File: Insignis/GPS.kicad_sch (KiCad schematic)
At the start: 4 parts, among them IC6 MAX-M10S-00B

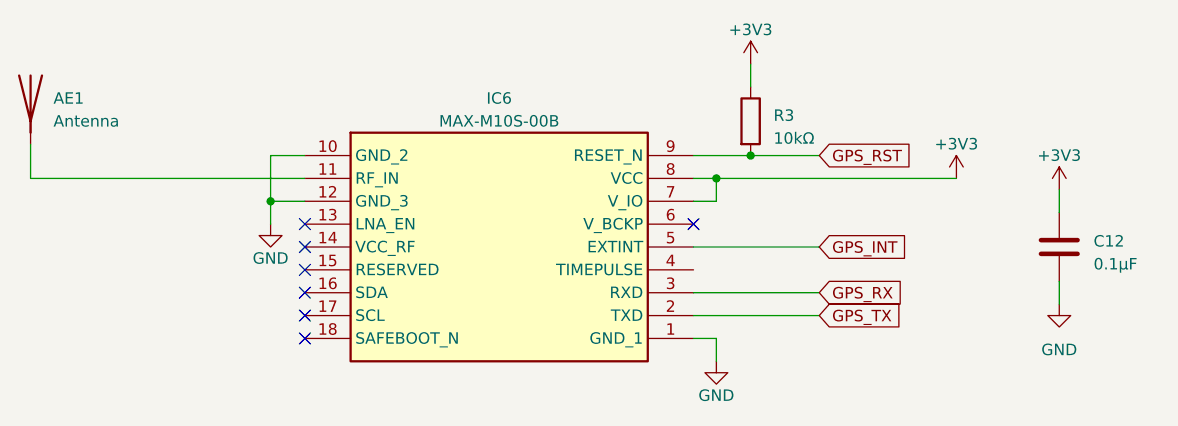
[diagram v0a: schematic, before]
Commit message: Fixed ERC errors
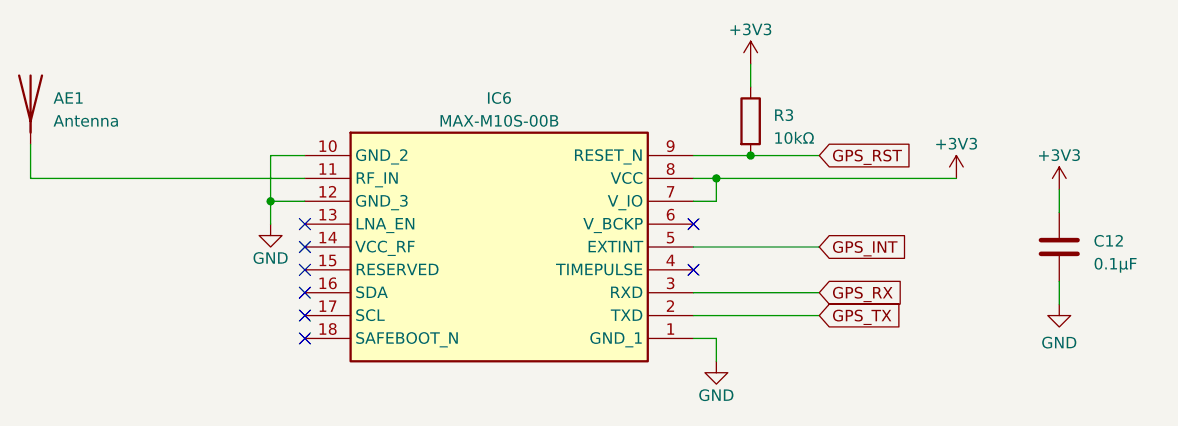
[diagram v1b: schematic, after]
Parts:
- IC6: footprint MAXM10S00B -> MAX-M10S-00B:MAXM10S00B
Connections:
- no-connect marks 7 -> 8
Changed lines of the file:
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@@
+	)
+	(no_connect
+		(at 158.75 92.71)
 	)
 	(no_connect
@@
 			)
 		)
-		(property "Description" ""
+		(property "Description" "Power symbol creates a global label with name \"+3V3\""
 			(at 165.1 69.85 0)
 			(effects
@@
 					(size 1.27 1.27)
 				)
+				(hide yes)
 			)
 		)
@@
 			)
 		)
-		(property "Footprint" "MAXM10S00B"
+		(property "Footprint" "MAX-M10S-00B:MAXM10S00B"
 			(at 154.94 174.93 0)
 			(effects
@@
 		(on_board yes)
 		(dnp no)
-		(fields_autoplaced yes)
 		(property "Reference" "#PWR030"
 			(at 199.39 102.87 0)
@@
 		)
 		(property "Value" "GND"
-			(at 199.39 101.6 0)
+			(at 199.39 100.838 0)
 			(effects
 				(font
@@
 			)
 		)
-		(property "Description" ""
+		(property "Description" "Power symbol creates a global label with name \"GND\" , ground"
 			(at 199.39 96.52 0)
 			(effects
@@
 					(size 1.27 1.27)
 				)
+				(hide yes)
 			)
 		)
@@
 			)
 		)
-		(property "Description" ""
+		(property "Description" "Power symbol creates a global label with name \"+3V3\""
 			(at 187.96 82.55 0)
 			(effects
@@
 					(size 1.27 1.27)
 				)
+				(hide yes)
 			)
 		)
@@
 			)
 		)
-		(property "Description" ""
+		(property "Description" "Power symbol creates a global label with name \"+3V3\""
 			(at 199.39 83.82 0)
 			(effects
@@
 					(size 1.27 1.27)
 				)
+				(hide yes)
 			)
 		)
@@
 			)
 		)
-		(property "Description" ""
+		(property "Description" "Power symbol creates a global label with name \"GND\" , ground"
 			(at 111.76 87.63 0)
 			(effects
@@
 					(size 1.27 1.27)
 				)
+				(hide yes)
 			)
 		)
@@
 			)
 		)
-		(property "Description" ""
+		(property "Description" "Power symbol creates a global label with name \"GND\" , ground"
 			(at 161.29 102.87 0)
 			(effects
@@
 					(size 1.27 1.27)
 				)
-			)
-		)
+				(hide yes)
+			)
+		)
